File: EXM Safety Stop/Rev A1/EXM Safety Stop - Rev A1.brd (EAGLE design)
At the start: 51.5 x 25.5 mm, 14 parts, among them J1 NC3FAV2, J102 22-05-7038-03, J2 NC3MAV, T100 EXMACHINA-LOGO-NAME

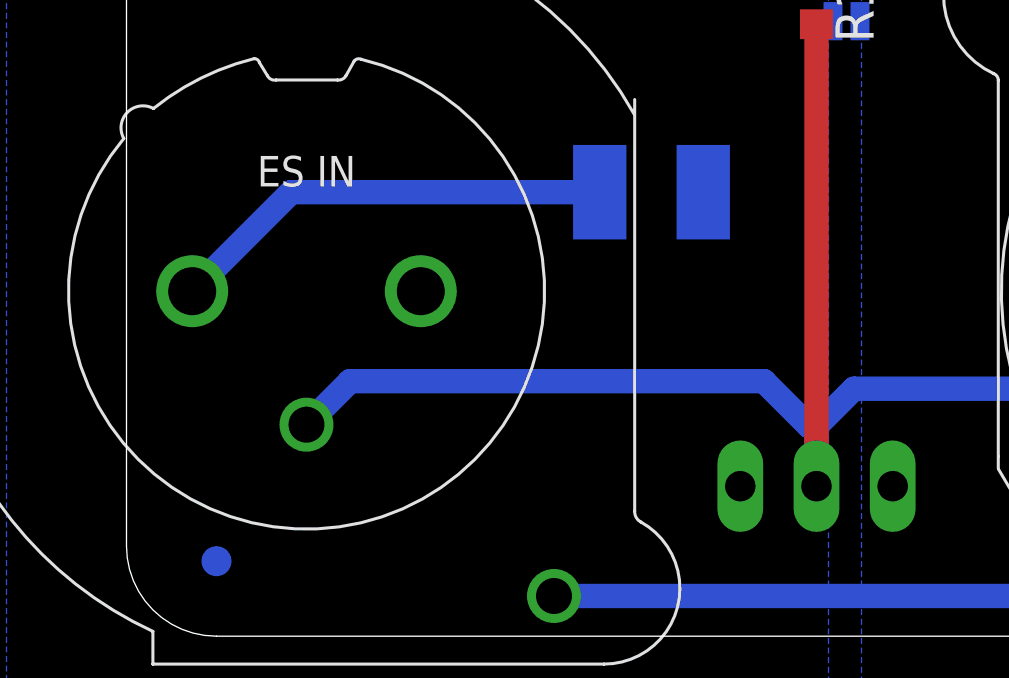
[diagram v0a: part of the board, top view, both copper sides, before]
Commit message: Final modifications before MDP in EXM Safety board - Rev A1:
- Renamed signal +24V_IN to +24V_PS
- Named signal +24V_IN
- Connect +24V_OUT after the fuse
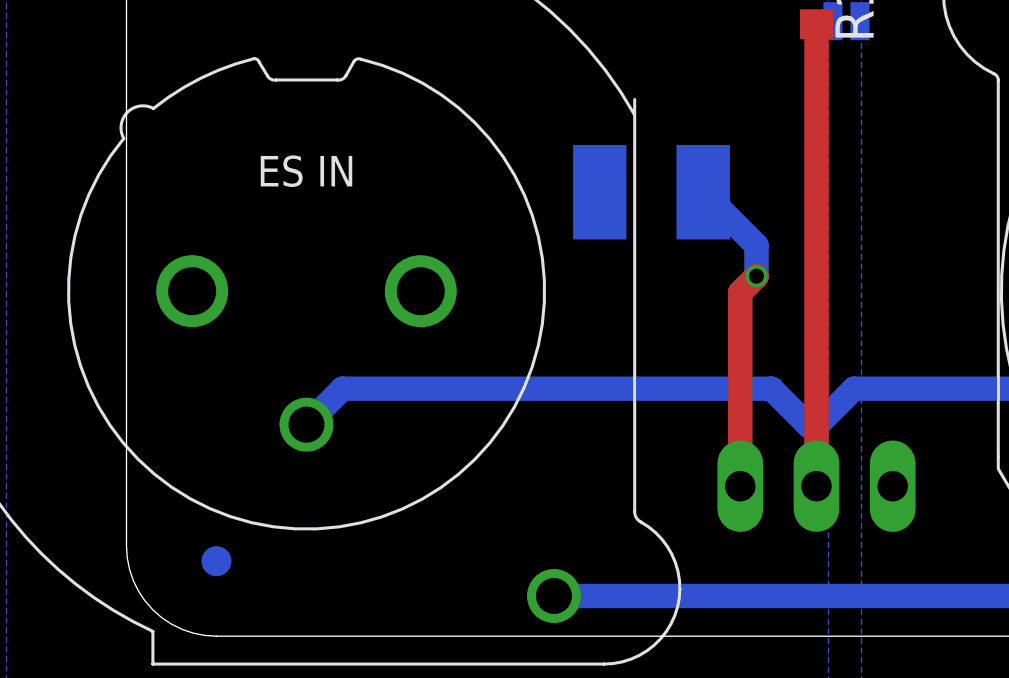
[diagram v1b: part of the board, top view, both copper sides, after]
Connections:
- removed net N$1: F100.1, J1.2
- new net +24V_PS: F100.2, J102.1
- net +24V_IN: now also F100.1, J1.2; no longer F100.2, J102.1
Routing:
- net N$1: track 15.0 -> 0.00 mm
- net +24V_PS: track 0.00 -> 11.4 mm, vias 0 -> 1
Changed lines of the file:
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@@
 <contactref element="J2" pad="3"/>
 <wire x1="23" y1="20.4" x2="23" y2="5" width="0.8128" layer="1"/>
-<wire x1="6" y1="7.05" x2="7.45" y2="8.5" width="0.8128" layer="16"/>
-<wire x1="7.45" y1="8.5" x2="21.25" y2="8.5" width="0.8128" layer="16"/>
+<wire x1="6" y1="7.05" x2="7.2" y2="8.25" width="0.8128" layer="16"/>
+<wire x1="7.2" y1="8.25" x2="21.5" y2="8.25" width="0.8128" layer="16"/>
 <wire x1="39.44" y1="8.25" x2="24.25" y2="8.25" width="0.8128" layer="16"/>
-<wire x1="23" y1="6" x2="23" y2="5" width="0.8128" layer="16"/>
-<wire x1="21.25" y1="8.5" x2="22.75" y2="7" width="0.8128" layer="16"/>
+<wire x1="21.5" y1="8.25" x2="22.75" y2="7" width="0.8128" layer="16"/>
 <wire x1="22.75" y1="7" x2="23" y2="7" width="0.8128" layer="16"/>
 <wire x1="39.44" y1="8.25" x2="40" y2="7.69" width="0.8128" layer="16"/>
 <wire x1="24.25" y1="8.25" x2="23" y2="7" width="0.8128" layer="16"/>
-<wire x1="23" y1="7" x2="23" y2="6" width="0.8128" layer="16"/>
+<wire x1="23" y1="7" x2="23" y2="5" width="0.8128" layer="16"/>
 </signal>
-<signal name="+24V_IN">
+<signal name="+24V_PS">
 <contactref element="F100" pad="2"/>
 <contactref element="J102" pad="1"/>
-<contactref element="SJ100" pad="2"/>
-<polygon width="0.8128" layer="16" isolate="0.3048">
-<vertex x="-4" y="26.5"/>
-<vertex x="23.4" y="26.5"/>
-<vertex x="23.4" y="-1.5"/>
-<vertex x="-4" y="-1.5"/>
-</polygon>
-</signal>
-<signal name="N$1">
-<contactref element="F100" pad="1"/>
-<contactref element="J1" pad="2"/>
-<wire x1="15.775" y1="14.8" x2="5.49" y2="14.8" width="0.8128" layer="16"/>
-<wire x1="5.49" y1="14.8" x2="2.19" y2="11.5" width="0.8128" layer="16"/>
+<wire x1="20.46" y1="5" x2="20.46" y2="11.46" width="0.8128" layer="1"/>
+<via x="21" y="12" extent="1-16" drill="0.5"/>
+<wire x1="20.54" y1="11.54" x2="21" y2="12" width="0.8128" layer="1"/>
+<wire x1="20.46" y1="11.46" x2="21" y2="12" width="0.8128" layer="1"/>
+<wire x1="21" y1="12" x2="21" y2="13.025" width="0.8128" layer="16"/>
+<wire x1="21" y1="13.025" x2="19.225" y2="14.8" width="0.8128" layer="16"/>
 </signal>
 <signal name="N$2">
@@
 <wire x1="38.095" y1="1.34" x2="40" y2="3.245" width="0.8128" layer="16"/>
 </signal>
+<signal name="+24V_IN">
+<polygon width="0.8128" layer="16" isolate="0.3048">
+<vertex x="-4" y="26.5"/>
+<vertex x="23.4" y="26.5"/>
+<vertex x="23.4" y="-1.5"/>
+<vertex x="-4" y="-1.5"/>
+</polygon>
+<contactref element="F100" pad="1"/>
+<contactref element="J1" pad="2"/>
+<contactref element="SJ100" pad="2"/>
+</signal>
 </signals>
